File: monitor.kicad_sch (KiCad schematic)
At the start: 50 parts, among them J1 Conn_01x01_Socket, J2 Conn_01x01_Socket, J3 Conn_01x01_Socket, J4 Conn_01x01_Socket, J5 Conn_01x01_Socket, J6 Conn_01x01_Socket, U704 OPA2197D, U71 TMUX6104, U72 TMUX6104, U76 OPA2189DGK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

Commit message: About to delete scan...
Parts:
- C701, C702: value 1n -> 330p; LCSC (none) -> C1664; now in the parts list
- C703: footprint Capacitor_SMD:C_0603_1608Metric -> Capacitor_SMD:C_0402_1005Metric
- C705: now in the parts list
- R702, R703: value 100 -> 330; LCSC C25076 -> C25104
- U704: Stock (none) -> 30
- U76, U78: Stock (none) -> 15
- U77: Stock (none) -> 14
- renumbered R704 to R71
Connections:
- net IN_A1: now also U71.5 (S2); no longer U71.4 (S1)
- net IN_A2: now also U71.11 (S3); no longer U71.5 (S2)
- net IN_A3: now also U71.10 (S4); no longer U71.11 (S3)
- net IN_B1: now also U72.5 (S2); no longer U72.4 (S1)
- net IN_B2: now also U72.11 (S3); no longer U72.5 (S2)
- net IN_B3: now also U72.10 (S4); no longer U72.11 (S3)

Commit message: Most blocks there....
About to restore scan.
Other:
- moved on the sheet: C705, JP71, R708, R713, R714, U78A, U78B

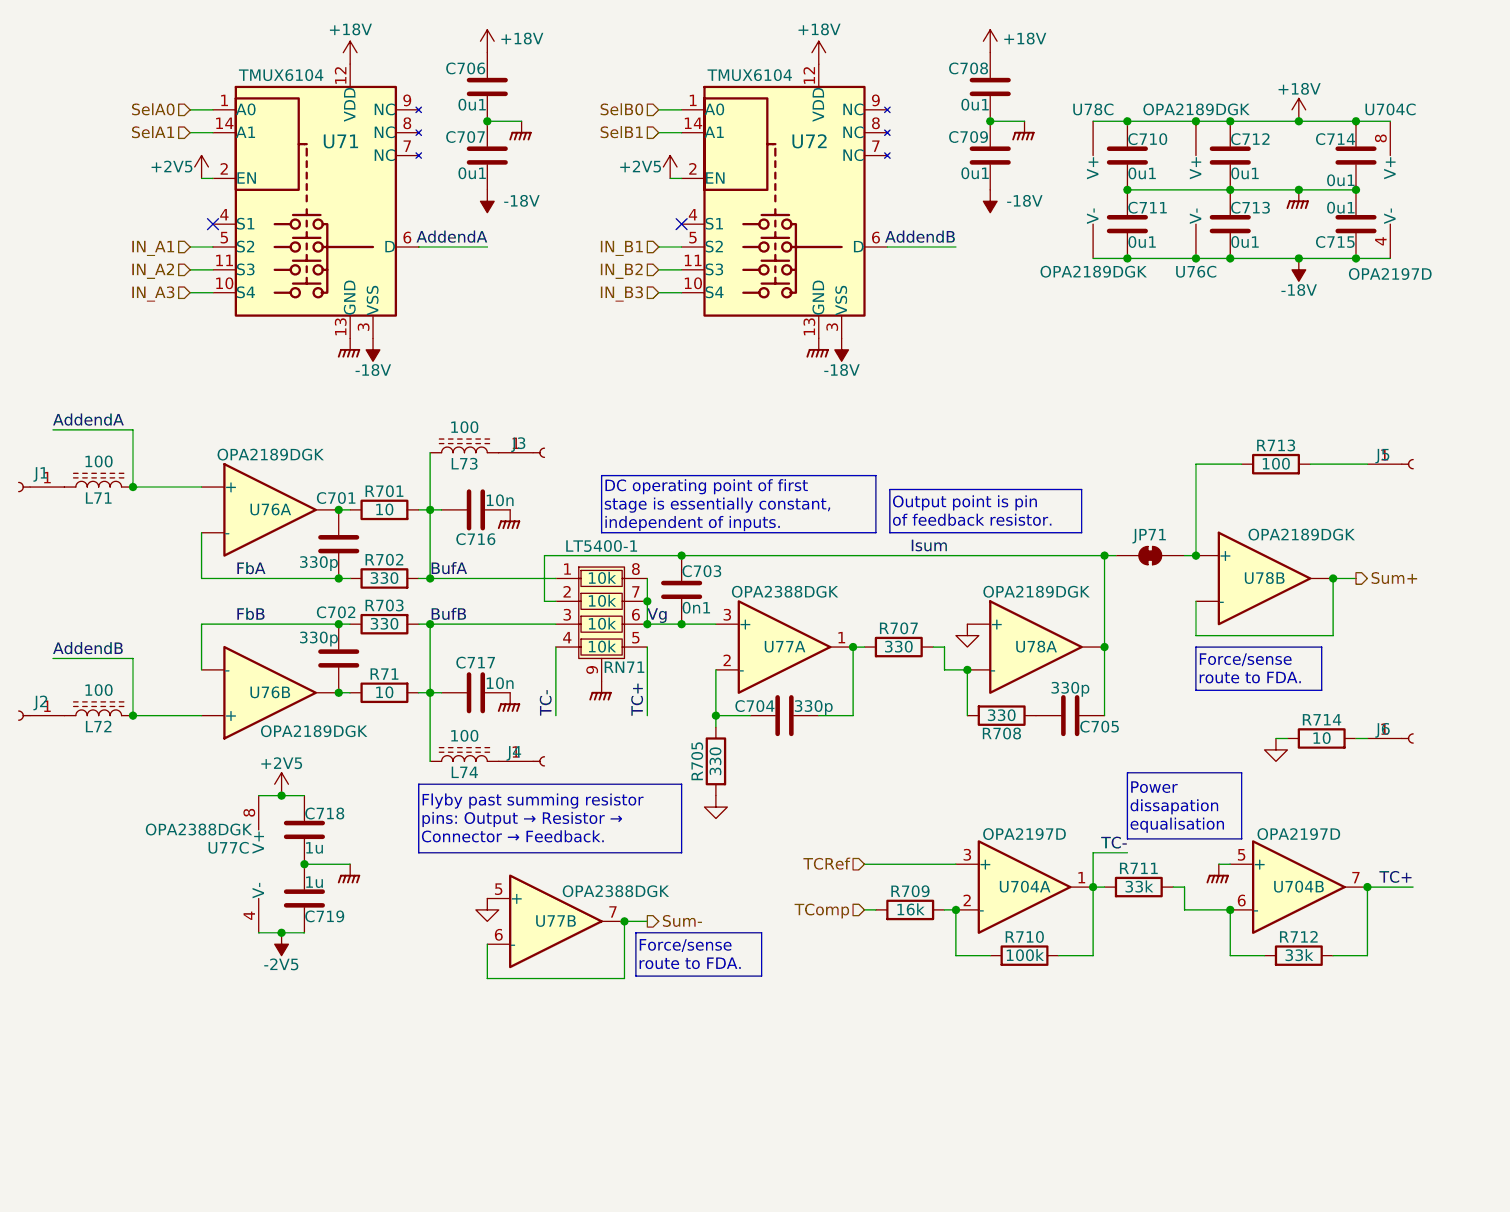
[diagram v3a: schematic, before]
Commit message: Put ref filtering into the schematic.
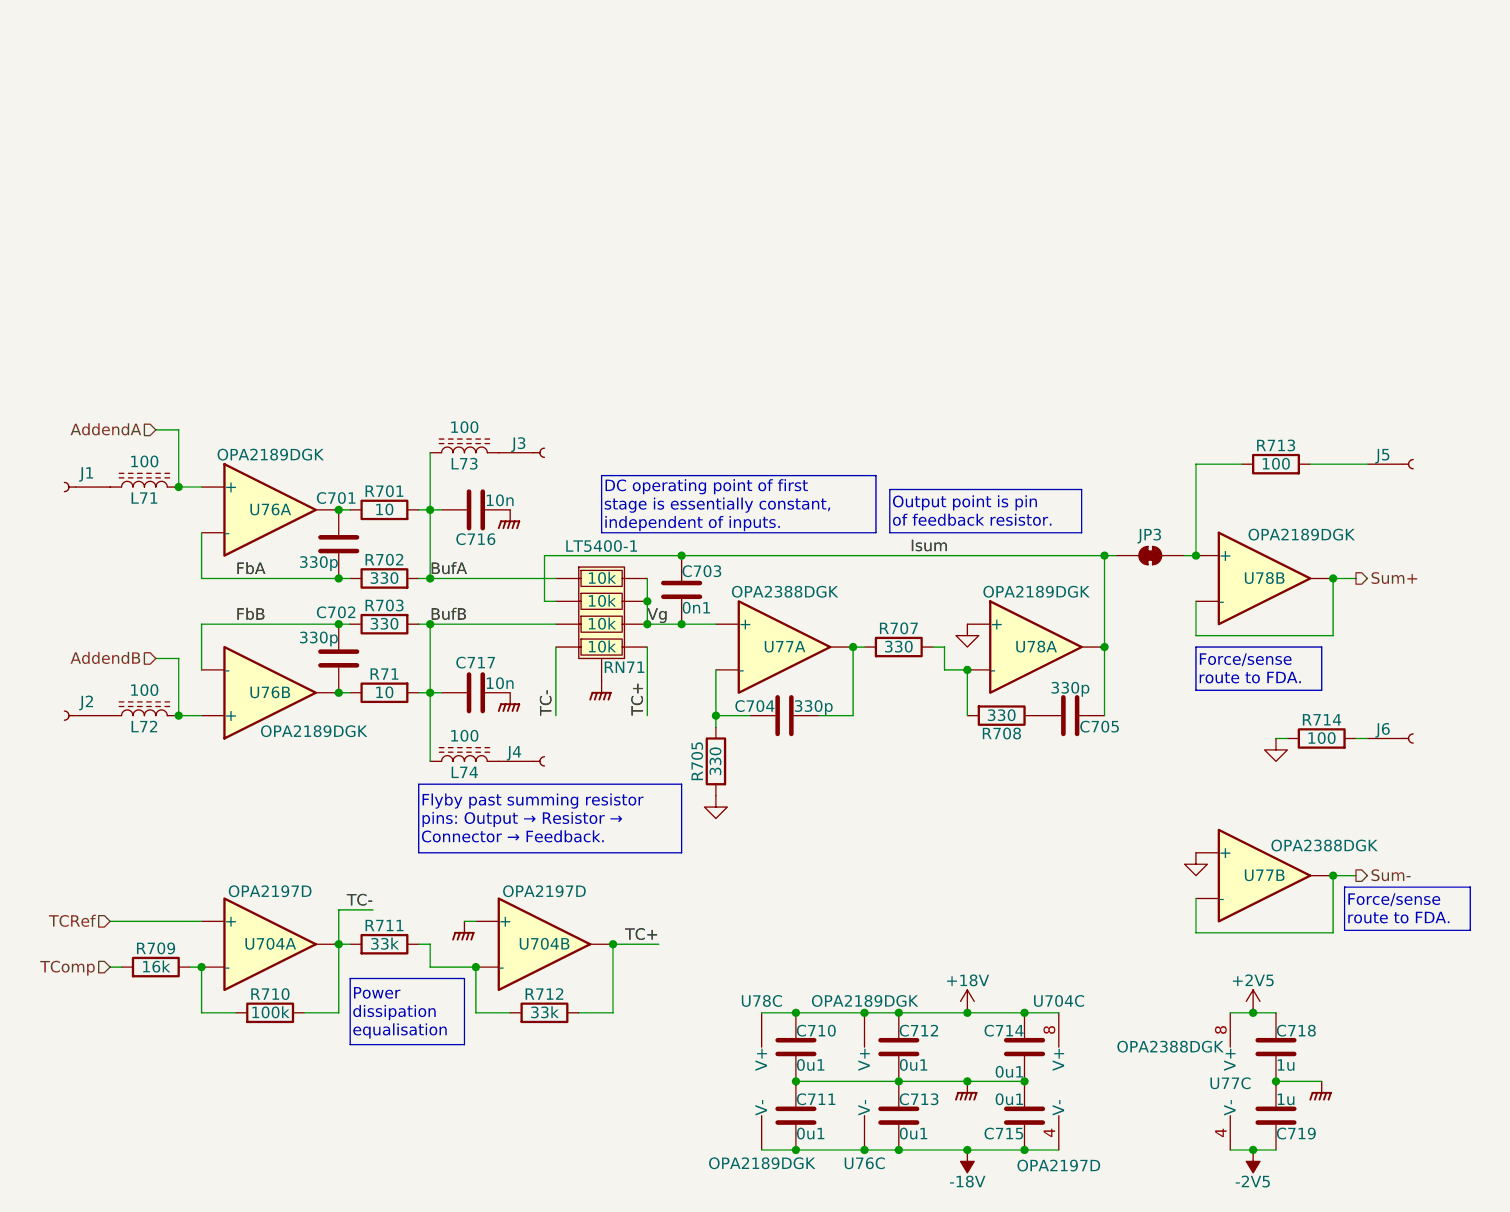
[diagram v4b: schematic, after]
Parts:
- removed C706, C707, C708, C709: 0u1, Capacitor_SMD:C_0402_1005Metric, symbol Device:C
- removed U71, U72: TMUX6104, Package_SO:TSSOP-14_4.4x5mm_P0.65mm, symbol Parts:TMUX6104
- R714: value 10 -> 100
- renumbered JP71 to JP3
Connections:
- no-connect marks 2 -> 0
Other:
- moved on the sheet: C710, C711, C712, C713, C714, C715, C718, C719, L71, L72, R709, R710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

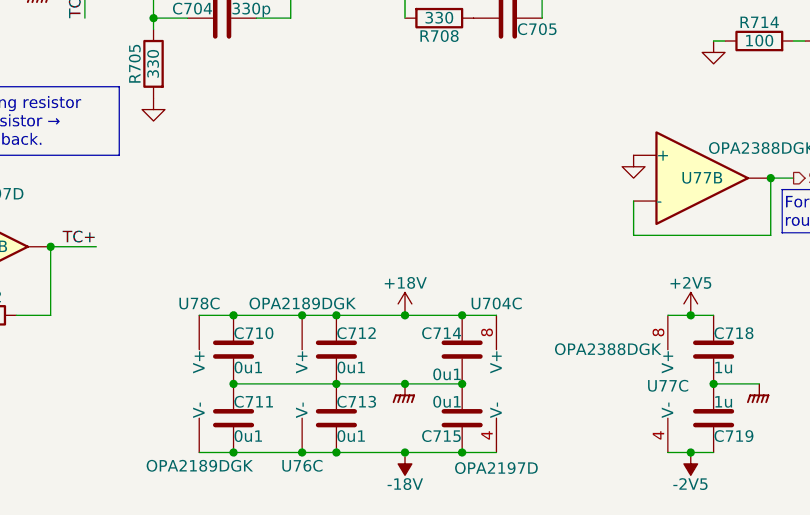
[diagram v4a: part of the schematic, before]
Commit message: Adjust voltage rails.
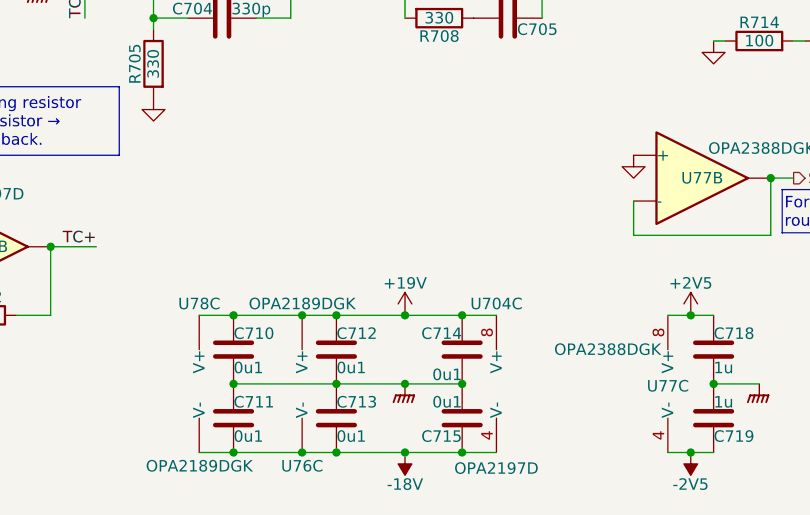
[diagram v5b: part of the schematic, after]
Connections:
- net +18V renamed +19V
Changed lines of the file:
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@@
 	)
 	(symbol
-		(lib_id "Parts:+18V")
+		(lib_id "Parts:+19V")
 		(at 179.07 128.27 0)
 		(unit 1)
@@
 		(on_board yes)
 		(dnp no)
-		(property "Reference" "#PWR0294"
+		(property "Reference" "#PWR294"
 			(at 179.07 132.08 0)
 			(effects
@@
 			)
 		)
-		(property "Value" "+18V"
+		(property "Value" "+19V"
 			(at 179.07 124.714 0)
 			(do_not_autoplace yes)
@@
 			)
 		)
-		(property "Description" "Power symbol creates a global label with name {dblquote}+18V{dblquote}"
+		(property "Description" "Power symbol creates a global label with name \"+19\""
 			(at 179.07 128.27 0)
 			(effects
@@
 			(project "lincal"
 				(path "/b054cef4-39e3-49d8-aff0-7ba5a206c187/b0f71c87-958f-452c-ba10-5bfb9905e5da"
-					(reference "#PWR0294")
+					(reference "#PWR294")
 					(unit 1)
 				)

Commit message: Progress checkin.  About to redo FDA feedback again.
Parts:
- removed R714: 100, Resistor_SMD:R_0402_1005Metric, symbol Device:R
- J1: value Conn_01x01_Socket -> A
- J2: value Conn_01x01_Socket -> B
- J3: value Conn_01x01_Socket -> Abuf
- J4: value Conn_01x01_Socket -> Bbuf
- J5: value Conn_01x01_Socket -> Sum
- J6: value Conn_01x01_Socket -> Gnd
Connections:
- net GND: now also J6.1 (Pin_1)
- net -18V renamed -16V
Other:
- moved on the sheet: J5, J6, JP3, R713, U77B, U78B

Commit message: Start to place within physical board size.
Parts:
- renumbered C711 to C710, C710 to C711
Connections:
- net +19V: now also C710.1; no longer C711.1
- net -16V: now also C711.2; no longer C710.2
- net GND: now also U78.5 (+); no longer U78.3 (+)
- net GNDPWR: now also C710.2, C711.1; no longer C710.1, C711.2
- net Isum: now also U78.7; no longer U78.1
- net Sum+: now also U78.1, U78.2 (-); no longer U78.6 (-), U78.7
- net at JP3.2 (B), R713.1: now also U78.3 (+); no longer U78.5 (+)
- net at R707.1, R708.2: now also U78.6 (-); no longer U78.2 (-)
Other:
- moved on the sheet: C710, C711
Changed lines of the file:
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@@
 		(lib_id "Parts:OPA2189DGK")
 		(at 209.55 80.01 0)
-		(unit 2)
+		(unit 1)
 		(exclude_from_sim no)
 		(in_bom no)
@@
 				(path "/b054cef4-39e3-49d8-aff0-7ba5a206c187/b0f71c87-958f-452c-ba10-5bfb9905e5da"
 					(reference "U78")
-					(unit 2)
+					(unit 1)
 				)
 			)
@@
 		(lib_id "Parts:OPA2189DGK")
 		(at 186.69 87.63 0)
-		(unit 1)
+		(unit 2)
 		(exclude_from_sim no)
 		(in_bom no)
@@
 				(path "/b054cef4-39e3-49d8-aff0-7ba5a206c187/b0f71c87-958f-452c-ba10-5bfb9905e5da"
 					(reference "U78")
-					(unit 1)
+					(unit 2)
 				)
 			)
@@
 	(symbol
 		(lib_id "Device:C")
-		(at 160.02 132.08 0)
+		(at 160.02 139.7 0)
 		(unit 1)
 		(exclude_from_sim no)
@@
 		(on_board yes)
 		(dnp no)
-		(property "Reference" "C710"
-			(at 160.02 130.302 0)
+		(property "Reference" "C711"
+			(at 160.02 137.922 0)
 			(effects
 				(font
@@
 		)
 		(property "Value" "0u1"
-			(at 160.02 134.112 0)
+			(at 160.02 141.732 0)
 			(effects
 				(font
@@
 		)
 		(property "Footprint" "Capacitor_SMD:C_0402_1005Metric"
-			(at 160.9852 135.89 0)
+			(at 160.9852 143.51 0)
 			(effects
 				(font
@@
 		)
 		(property "Datasheet" "X7R, 50V"
-			(at 160.02 132.08 0)
+			(at 160.02 139.7 0)
 			(effects
 				(font
@@
 		)
 		(property "Description" "Unpolarized capacitor"
-			(at 160.02 132.08 0)
+			(at 160.02 139.7 0)
 			(effects
 				(font
@@
 		)
 		(property "LCSC" "C307331"
-			(at 160.02 132.08 0)
+			(at 160.02 139.7 0)
 			(effects
 				(font
@@
 		)
 		(property "Stock" ""
-			(at 160.02 132.08 0)
+			(at 160.02 139.7 0)
 			(effects
 				(font
@@
 			(project "lincal"
 				(path "/b054cef4-39e3-49d8-aff0-7ba5a206c187/b0f71c87-958f-452c-ba10-5bfb9905e5da"
-					(reference "C710")
+					(reference "C711")
 					(unit 1)
 				)
@@
 	(symbol
 		(lib_id "Device:C")
-		(at 160.02 139.7 0)
+		(at 160.02 132.08 0)
 		(unit 1)
 		(exclude_from_sim no)
@@
 		(on_board yes)
 		(dnp no)
-		(property "Reference" "C711"
-			(at 160.02 137.922 0)
+		(property "Reference" "C710"
+			(at 160.02 130.302 0)
 			(effects
 				(font
@@
 		)
 		(property "Value" "0u1"
-			(at 160.02 141.732 0)
+			(at 160.02 134.112 0)
 			(effects
 				(font
@@
 		)
 		(property "Footprint" "Capacitor_SMD:C_0402_1005Metric"
-			(at 160.9852 143.51 0)
+			(at 160.9852 135.89 0)
 			(effects
 				(font
@@
 		)
 		(property "Datasheet" "X7R, 50V"
-			(at 160.02 139.7 0)
+			(at 160.02 132.08 0)
 			(effects
 				(font
@@
 		)
 		(property "Description" "Unpolarized capacitor"
-			(at 160.02 139.7 0)
+			(at 160.02 132.08 0)
 			(effects
 				(font
@@
 		)
 		(property "LCSC" "C307331"
-			(at 160.02 139.7 0)
+			(at 160.02 132.08 0)
 			(effects
 				(font
@@
 		)
 		(property "Stock" ""
-			(at 160.02 139.7 0)
+			(at 160.02 132.08 0)
 			(effects
 				(font
@@
 			(project "lincal"
 				(path "/b054cef4-39e3-49d8-aff0-7ba5a206c187/b0f71c87-958f-452c-ba10-5bfb9905e5da"
-					(reference "C711")
+					(reference "C710")
 					(unit 1)
 				)

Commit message: Power mostly routed
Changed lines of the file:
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@@
 		)
 	)
-	(text_box "Flyby past summing resistor pins: Output → Resistor → Connector → Feedback."
+	(text_box "Flyby past summing resistor pins: Drive → Resistor → Connection → Sense."
 		(exclude_from_sim no)
 		(at 118.11 102.87 0)
